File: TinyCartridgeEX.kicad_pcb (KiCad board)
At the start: 2 copper layers, 62 x 81.1 mm, 25 parts, among them U1 SN74LVC8T245, U2 SN74LVC8T245, U3 SN74LVC8T245, U4 74LV17A, U5 74LVC06A, U6 74LVC1G06, U7 74LVC2G132, U9 TinyFPGA_EX, X1 EXPANSION_PORT_C64_EDGE

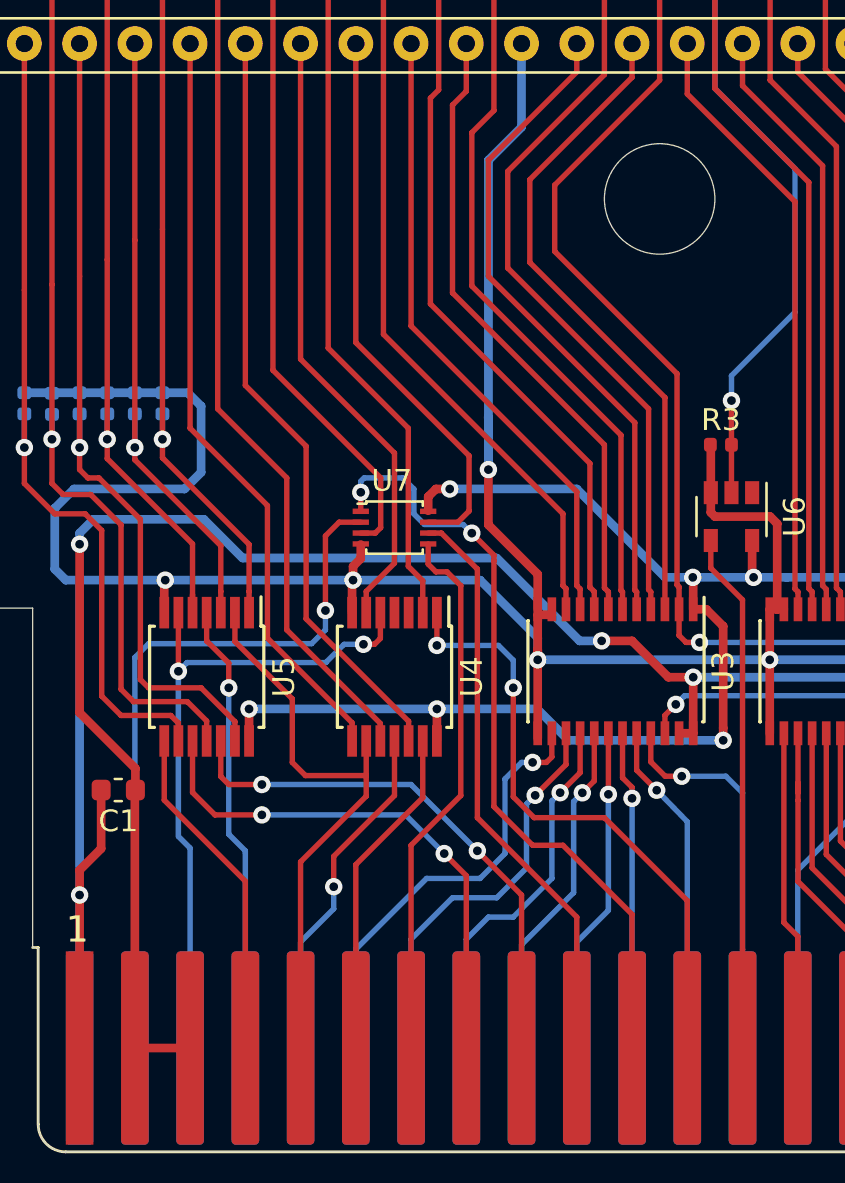
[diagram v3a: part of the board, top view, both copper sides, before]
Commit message: Replace cartridge footprint
The new footprint is created based on the technical drawings
found here:  http://wiki.icomp.de/wiki/C64_Cartridge_Cases
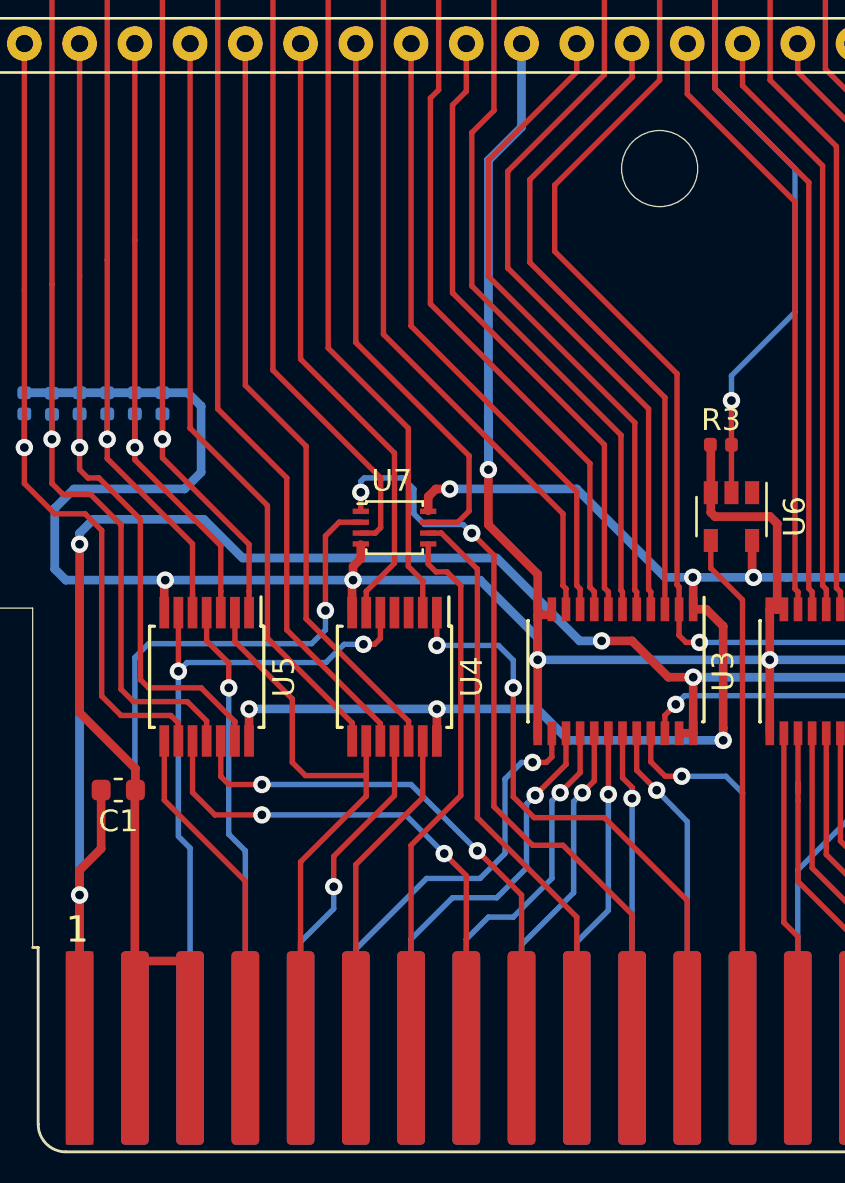
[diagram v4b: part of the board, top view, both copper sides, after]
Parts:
- CART1: footprint RETRO_Innovations:CARTRIDGE_C64 -> icomp:CARTRIDGE_C64_GERMAN
- moved CART1 45.2 mm to (76.2, 119.9)
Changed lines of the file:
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@@
     (add_net VCC)
+  )
+  (module icomp:CARTRIDGE_C64_GERMAN (layer F.Cu)
+    (at 76.2 119.888)
+    (fp_text reference CART1 (at 0 0) (layer F.SilkS) hide
+      (effects (font (size 1.27 1.27) (thickness 0.15)))
+    )
+    (fp_text value CARTRIDGE_C64 (at 0 0) (layer F.SilkS) hide
+      (effects (font (size 1.27 1.27) (thickness 0.15)))
+    )
+    (fp_circle (center 0 0) (end 2.575 0) (layer F.CrtYd) (width 1))
+    (fp_line (start -32.9 45.4) (end -32.9 -39.9) (layer Dwgs.User) (width 2.2))
+    (fp_line (start -32.9 -39.9) (end 32.9 -39.9) (layer Dwgs.User) (width 2.2))
+    (fp_line (start 32.9 -39.9) (end 32.9 45.4) (layer Dwgs.User) (width 2.2))
+    (fp_line (start 32.9 45.4) (end -32.9 45.4) (layer Dwgs.User) (width 2.2))
+    (fp_line (start -33.1 36.4) (end 33.1 36.4) (layer Dwgs.User) (width 1.8))
+    (fp_line (start -33.35 -33.85) (end -29.65 -33.85) (layer Dwgs.User) (width 1.3))
+    (fp_line (start -29.65 -33.85) (end -29.65 -24.15) (layer Dwgs.User) (width 1.3))
+    (fp_line (start -29.65 -24.15) (end -33.35 -24.15) (layer Dwgs.User) (width 1.3))
+    (fp_line (start -33.35 -24.15) (end -33.35 -33.85) (layer Dwgs.User) (width 1.3))
+    (fp_line (start -33.35 24.15) (end -29.65 24.15) (layer Dwgs.User) (width 1.3))
+    (fp_line (start -29.65 24.15) (end -29.65 33.85) (layer Dwgs.User) (width 1.3))
+    (fp_line (start -29.65 33.85) (end -33.35 33.85) (layer Dwgs.User) (width 1.3))
+    (fp_line (start -33.35 33.85) (end -33.35 24.15) (layer Dwgs.User) (width 1.3))
+    (fp_line (start 33.35 -33.85) (end 29.65 -33.85) (layer Dwgs.User) (width 1.3))
+    (fp_line (start 29.65 -33.85) (end 29.65 -24.15) (layer Dwgs.User) (width 1.3))
+    (fp_line (start 29.65 -24.15) (end 33.35 -24.15) (layer Dwgs.User) (width 1.3))
+    (fp_line (start 33.35 -24.15) (end 33.35 -33.85) (layer Dwgs.User) (width 1.3))
+    (fp_line (start 33.35 24.15) (end 29.65 24.15) (layer Dwgs.User) (width 1.3))
+    (fp_line (start 29.65 24.15) (end 29.65 33.85) (layer Dwgs.User) (width 1.3))
+    (fp_line (start 29.65 33.85) (end 33.35 33.85) (layer Dwgs.User) (width 1.3))
+    (fp_line (start 33.35 33.85) (end 33.35 24.15) (layer Dwgs.User) (width 1.3))
+    (pad "" np_thru_hole circle (at 0 0) (size 3.5 3.5) (drill 3.5) (layers *.Cu *.Mask))
   )
   (module Symbol:Symbol_CC-Attribution_CopperTop_Small (layer F.Cu)
@@
       (effects (font (size 1 1) (thickness 0.15)))
     )
-    (fp_text value Symbol_CC-Attribution_CopperTop_Small (at 0 4.064) (layer F.Fab)
+    (fp_text value Symbol_CC-Attribution_CopperTop_Small (at 0 4.064) (layer F.Fab) hide
       (effects (font (size 1 1) (thickness 0.15)))
     )
@@
       (effects (font (size 1 1) (thickness 0.15)))
     )
-    (fp_text value Symbol_CreativeCommons_CopperTop_Type2_Small (at 0.127 3.683) (layer F.Fab)
+    (fp_text value Symbol_CreativeCommons_CopperTop_Type2_Small (at 0.127 3.683) (layer F.Fab) hide
       (effects (font (size 1 1) (thickness 0.15)))
     )
@@
       (effects (font (size 1 1) (thickness 0.15)))
     )
-    (fp_text value Symbol_CC-ShareAlike_CopperTop_Small (at 0.508 3.81) (layer F.Fab)
+    (fp_text value Symbol_CC-ShareAlike_CopperTop_Small (at 0.508 3.81) (layer F.Fab) hide
       (effects (font (size 1 1) (thickness 0.15)))
     )
@@
     (fp_line (start -1.09982 1.19888) (end -0.59944 1.50114) (layer F.Cu) (width 0.381))
   )
-  (module RETRO_Innovations:CARTRIDGE_C64 (layer F.Cu)
-    (at 76.2 165.1)
-    (fp_text reference CART1 (at 0 0) (layer F.SilkS) hide
-      (effects (font (size 1.27 1.27) (thickness 0.15)))
-    )
-    (fp_text value CARTRIDGE_C64 (at 0 0) (layer F.SilkS) hide
-      (effects (font (size 1.27 1.27) (thickness 0.15)))
-    )
-    (fp_line (start -34.036 0) (end -31.4325 0) (layer Dwgs.User) (width 0.1))
-    (fp_line (start 31.4325 0) (end 34.036 0) (layer Dwgs.User) (width 0.1))
-    (fp_line (start 34.036 0) (end 34.036 -88.138) (layer Dwgs.User) (width 0.1))
-    (fp_line (start 34.036 -88.138) (end -34.036 -88.138) (layer Dwgs.User) (width 0.1))
-    (fp_line (start -34.036 -88.138) (end -34.036 0) (layer Dwgs.User) (width 0.1))
-    (fp_line (start -31.4325 -86.106) (end 31.4325 -86.106) (layer Dwgs.User) (width 0.1))
-    (fp_line (start 31.4325 -86.106) (end 31.4325 -77.5208) (layer Dwgs.User) (width 0.1))
-    (fp_line (start 31.4325 -77.5208) (end 28.8925 -77.5208) (layer Dwgs.User) (width 0.1))
-    (fp_line (start 28.8925 -77.5208) (end 28.8925 -74.295) (layer Dwgs.User) (width 0.1))
-    (fp_line (start 28.8925 -74.295) (end 31.4325 -74.295) (layer Dwgs.User) (width 0.1))
-    (fp_line (start 31.4325 -74.295) (end 31.4325 -20.1168) (layer Dwgs.User) (width 0.1))
-    (fp_line (start 31.4325 -20.1168) (end 28.8925 -20.1168) (layer Dwgs.User) (width 0.1))
-    (fp_line (start 28.8925 -20.1168) (end 28.8925 -17.526) (layer Dwgs.User) (width 0.1))
-    (fp_line (start 28.8925 -17.526) (end 31.4325 -17.526) (layer Dwgs.User) (width 0.1))
-    (fp_line (start 31.4325 -17.526) (end 31.4325 0) (layer Dwgs.User) (width 0.1))
-    (fp_line (start 31.4325 0) (end -31.4325 0) (layer Dwgs.User) (width 0.1))
-    (fp_line (start -31.4325 0) (end -31.4325 -17.526) (layer Dwgs.User) (width 0.1))
-    (fp_line (start -31.4325 -17.526) (end -28.8925 -17.526) (layer Dwgs.User) (width 0.1))
-    (fp_line (start -28.8925 -17.526) (end -28.8925 -20.1168) (layer Dwgs.User) (width 0.1))
-    (fp_line (start -28.8925 -20.1168) (end -31.4325 -20.1168) (layer Dwgs.User) (width 0.1))
-    (fp_line (start -31.4325 -20.1168) (end -31.4325 -74.295) (layer Dwgs.User) (width 0.1))
-    (fp_line (start -31.4325 -74.295) (end -28.8925 -74.295) (layer Dwgs.User) (width 0.1))
-    (fp_line (start -28.8925 -74.295) (end -28.8925 -77.5208) (layer Dwgs.User) (width 0.1))
-    (fp_line (start -28.8925 -77.5208) (end -31.4325 -77.5208) (layer Dwgs.User) (width 0.1))
-    (fp_line (start -31.4325 -77.5208) (end -31.4325 -86.106) (layer Dwgs.User) (width 0.1))
-    (pad "" np_thru_hole circle (at 0 -43.815) (size 5.08 5.08) (drill 5.08) (layers *.Cu *.Mask))
-  )
   (module Package_SO:VSSOP-8_2.4x2.1mm_P0.5mm (layer F.Cu)
     (at 64.008 136.398)
@@
       (effects (font (size 1 1) (thickness 0.15)))
     )
-    (fp_text value 74LVC2G132 (at 0 2.413) (layer F.Fab)
+    (fp_text value 74LVC2G132 (at -0.008 -2.098) (layer F.Fab)
       (effects (font (size 1 1) (thickness 0.15)))
     )
@@
       (effects (font (size 1 1) (thickness 0.15)))
     )
-    (fp_text value 4.7k (at 0 -1.27) (layer F.Fab)
+    (fp_text value 4.7k (at -0.083 1.088) (layer F.Fab)
       (effects (font (size 1 1) (thickness 0.15)))
     )
@@
       (effects (font (size 1 1) (thickness 0.15)))
     )
-    (fp_text value 4.7k (at -0.104 -1.27) (layer F.Fab)
+    (fp_text value 4.7k (at -0.023 1.014) (layer F.Fab)
       (effects (font (size 1 1) (thickness 0.15)))
     )
@@
       (effects (font (size 1 1) (thickness 0.15)))
     )
-    (fp_text value 4.7k (at 0 1.17) (layer F.Fab)
+    (fp_text value 4.7k (at 0.001 -1.141) (layer F.Fab)
       (effects (font (size 1 1) (thickness 0.15)))
     )
@@
       (effects (font (size 1 1) (thickness 0.15)))
     )
-    (fp_text value 0.1u (at 0 1.43) (layer F.Fab)
+    (fp_text value 0.1u (at 0.008 -1.437) (layer F.Fab)
       (effects (font (size 1 1) (thickness 0.15)))
     )
@@
       (effects (font (size 1 1) (thickness 0.15)))
     )
-    (fp_text value 74LVC1G06 (at 0 2.9 90) (layer F.Fab)
+    (fp_text value 74LVC1G06 (at -1.69 0.002 180) (layer F.Fab)
       (effects (font (size 1 1) (thickness 0.15)))
     )
@@
   (gr_line (start 47.371 155.702) (end 47.625 155.702) (layer Edge.Cuts) (width 0.05))
   (gr_line (start 104.775 155.702) (end 105.029 155.702) (layer Edge.Cuts) (width 0.05))
-  (segment (start 52.07 160.3248) (end 54.61 160.3248) (width 0.4) (layer F.Cu) (net 1))
   (segment (start 77.093 145.852) (end 77.743 145.852) (width 0.4) (layer F.Cu) (net 1))
   (segment (start 87.761 145.852) (end 88.411 145.852) (width 0.4) (layer F.Cu) (net 1))
@@
   (segment (start 49.53 137.16) (end 49.53 144.907) (width 0.4) (layer F.Cu) (net 1))
   (segment (start 55.245 136.017) (end 57.023 137.795) (width 0.4) (layer B.Cu) (net 1))
+  (segment (start 52.07 156.3248) (end 54.61 156.3248) (width 0.4) (layer F.Cu) (net 1))
   (segment (start 91.929 140.406) (end 92.579 140.406) (width 0.4) (layer F.Cu) (net 2))
   (segment (start 81.261 142.475) (end 81.261 145.852) (width 0.4) (layer F.Cu) (net 2))

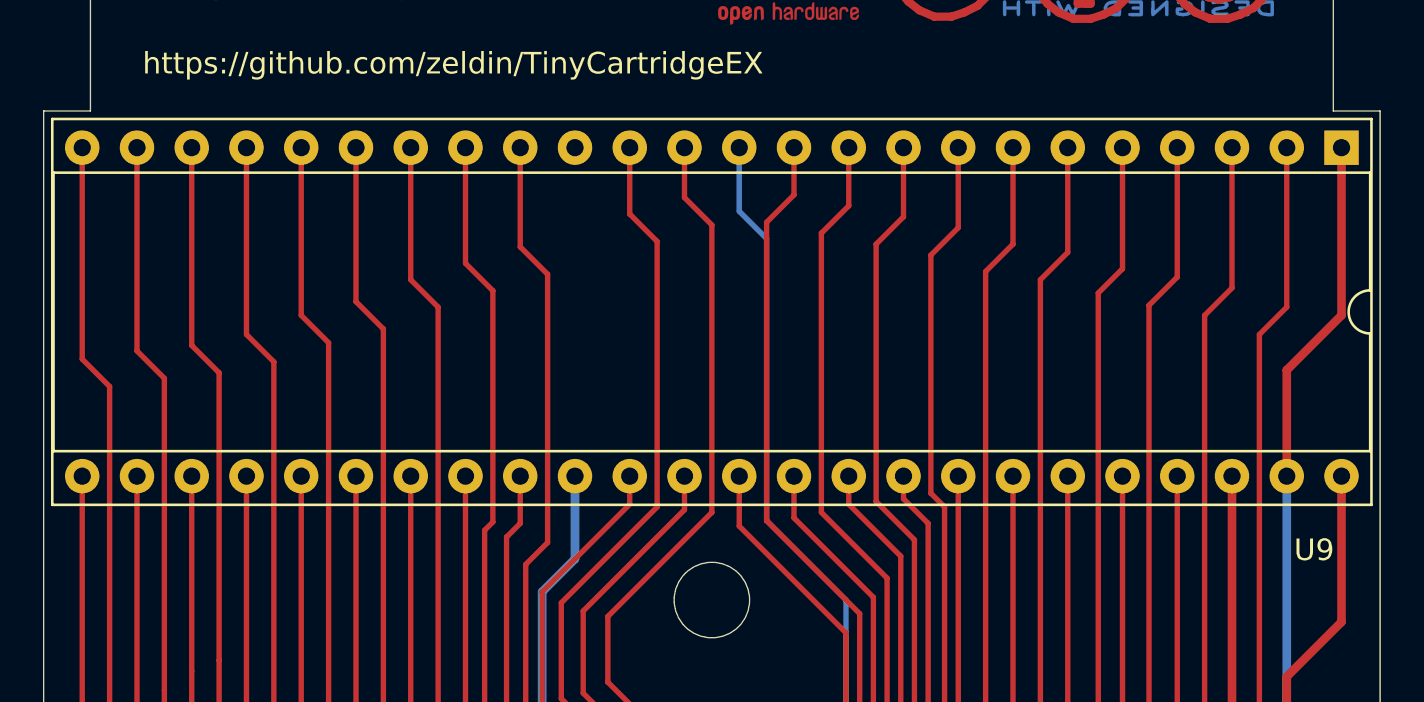
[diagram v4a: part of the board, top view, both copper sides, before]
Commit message: Insert a 3D model of the TinyFPGA EX module
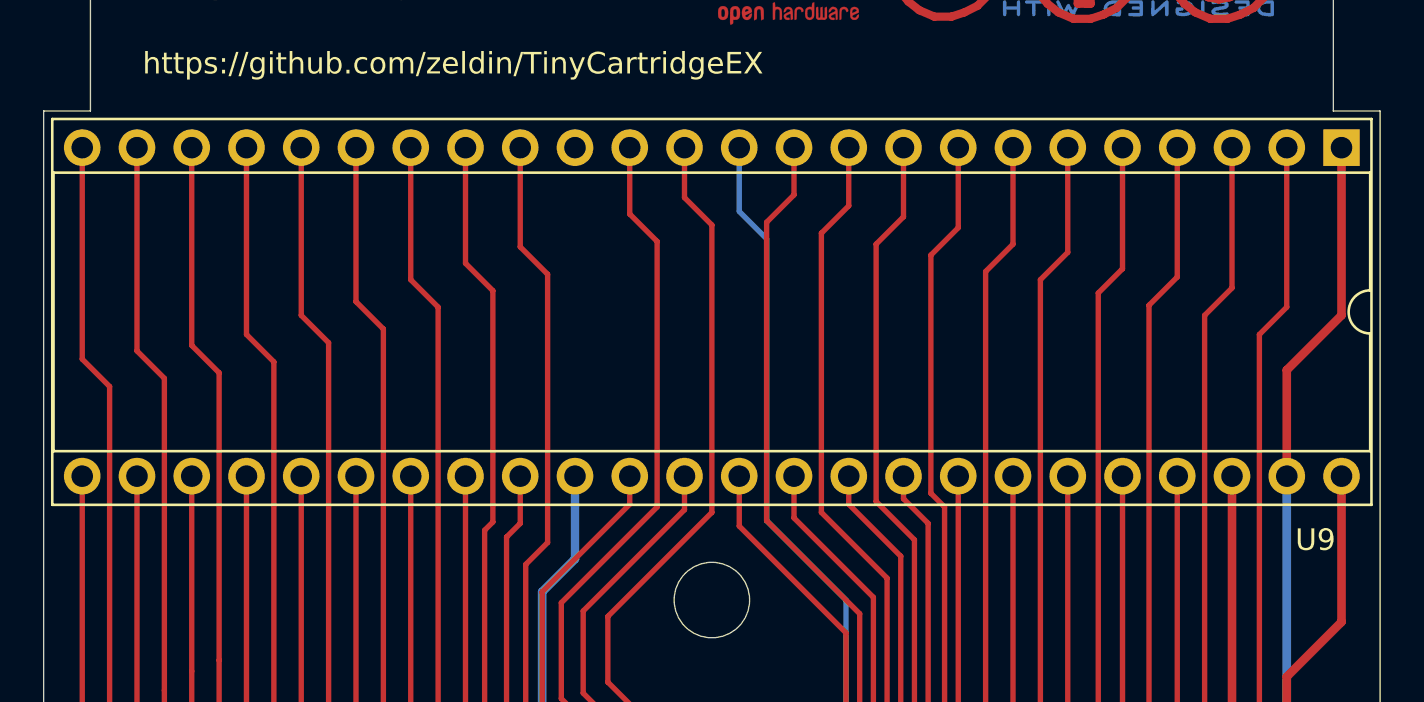
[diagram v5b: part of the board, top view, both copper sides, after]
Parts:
- added J1: Conn_01x24, PinHeader:PinHeader_1x24_P2.54mm_Vertical_UpsideDown, F.Cu at (105.4, 98.9)
- added J2: Conn_01x24, PinHeader:PinHeader_1x24_P2.54mm_Vertical_UpsideDown, F.Cu at (47.0, 114.1)
- U9: footprint Package_DIP:DIP-48_W15.24mm_Socket -> TinyFPGA:TinyFPGA_EX

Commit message: Add diode to Vin
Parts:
- added D1: EC30QSA045, Diode_SMD:D_SMA_Handsoldering, F.Cu at (104.3, 127.2)
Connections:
- U9 pad 48: +5V -> Net-(D1-Pad1)
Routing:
- net +5V: track 123.3 -> 107.2 mm
- net Net-(D1-Pad1): track 0.00 -> 11.0 mm
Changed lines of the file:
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@@
     (thickness 1.6)
     (drawings 20)
-    (tracks 723)
+    (tracks 726)
     (zones 0)
-    (modules 27)
-    (nets 85)
+    (modules 28)
+    (nets 86)
   )
   (page A4)
@@
   (net 83 "Net-(U7-Pad2)")
   (net 84 "Net-(U7-Pad1)")
+  (net 85 "Net-(D1-Pad1)")
   (net_class Default "This is the default net class."
     (clearance 0.2)
@@
     (add_net +5V)
     (add_net GND)
+    (add_net "Net-(D1-Pad1)")
     (add_net VCC)
+  )
+  (module Diode_SMD:D_SMA_Handsoldering (layer F.Cu)
+    (at 104.3 127.2 270)
+    (descr "Diode SMA (DO-214AC) Handsoldering")
+    (tags "Diode SMA (DO-214AC) Handsoldering")
+    (attr smd)
+    (fp_text reference D1 (at -0.2 2.5 90) (layer F.SilkS)
+      (effects (font (size 1 1) (thickness 0.15)))
+    )
+    (fp_text value EC30QSA045 (at 0 2.6 90) (layer F.Fab)
+      (effects (font (size 1 1) (thickness 0.15)))
+    )
+    (fp_line (start -4.4 -1.65) (end 2.5 -1.65) (layer F.SilkS) (width 0.12))
+    (fp_line (start -4.4 1.65) (end 2.5 1.65) (layer F.SilkS) (width 0.12))
+    (fp_line (start -0.64944 0.00102) (end 0.50118 -0.79908) (layer F.Fab) (width 0.1))
+    (fp_line (start -0.64944 0.00102) (end 0.50118 0.75032) (layer F.Fab) (width 0.1))
+    (fp_line (start 0.50118 0.75032) (end 0.50118 -0.79908) (layer F.Fab) (width 0.1))
+    (fp_line (start -0.64944 -0.79908) (end -0.64944 0.80112) (layer F.Fab) (width 0.1))
+    (fp_line (start 0.50118 0.00102) (end 1.4994 0.00102) (layer F.Fab) (width 0.1))
+    (fp_line (start -0.64944 0.00102) (end -1.55114 0.00102) (layer F.Fab) (width 0.1))
+    (fp_line (start -4.5 1.75) (end -4.5 -1.75) (layer F.CrtYd) (width 0.05))
+    (fp_line (start 4.5 1.75) (end -4.5 1.75) (layer F.CrtYd) (width 0.05))
+    (fp_line (start 4.5 -1.75) (end 4.5 1.75) (layer F.CrtYd) (width 0.05))
+    (fp_line (start -4.5 -1.75) (end 4.5 -1.75) (layer F.CrtYd) (width 0.05))
+    (fp_line (start 2.3 -1.5) (end -2.3 -1.5) (layer F.Fab) (width 0.1))
+    (fp_line (start 2.3 -1.5) (end 2.3 1.5) (layer F.Fab) (width 0.1))
+    (fp_line (start -2.3 1.5) (end -2.3 -1.5) (layer F.Fab) (width 0.1))
+    (fp_line (start 2.3 1.5) (end -2.3 1.5) (layer F.Fab) (width 0.1))
+    (fp_line (start -4.4 -1.65) (end -4.4 1.65) (layer F.SilkS) (width 0.12))
+    (fp_text user %R (at 0 -2.5 90) (layer F.Fab)
+      (effects (font (size 1 1) (thickness 0.15)))
+    )
+    (pad 2 smd rect (at 2.5 0 270) (size 3.5 1.8) (layers F.Cu F.Paste F.Mask)
+      (net 1 +5V))
+    (pad 1 smd rect (at -2.5 0 270) (size 3.5 1.8) (layers F.Cu F.Paste F.Mask)
+      (net 85 "Net-(D1-Pad1)"))
+    (model ${KISYS3DMOD}/Diode_SMD.3dshapes/D_SMA.wrl
+      (at (xyz 0 0 0))
+      (scale (xyz 1 1 1))
+      (rotate (xyz 0 0 0))
+    )
   )
   (module TinyFPGA:TinyFPGA_EX (layer F.Cu)
@@
     (fp_arc (start 7.62 -1.33) (end 6.62 -1.33) (angle -180) (layer F.SilkS) (width 0.12))
     (pad 48 thru_hole oval (at 15.24 0 270) (size 1.7 1.7) (drill 1) (layers *.Cu *.Mask)
-      (net 1 +5V))
+      (net 85 "Net-(D1-Pad1)"))
     (pad 24 thru_hole oval (at 0 58.42 270) (size 1.7 1.7) (drill 1) (layers *.Cu *.Mask)
       (net 65 GAME))
@@
   (segment (start 52.07 148.4885) (end 52.0955 148.463) (width 0.4) (layer F.Cu) (net 1))
   (segment (start 52.07 160.3248) (end 52.07 148.4885) (width 0.4) (layer F.Cu) (net 1))
-  (segment (start 102.87 141.986) (end 101.581 143.275) (width 0.4) (layer F.Cu) (net 1))
-  (segment (start 101.581 143.275) (end 99.079 143.275) (width 0.4) (layer F.Cu) (net 1))
-  (segment (start 102.87 123.444) (end 102.87 141.986) (width 0.4) (layer F.Cu) (net 1))
-  (segment (start 105.41 120.904) (end 102.87 123.444) (width 0.4) (layer F.Cu) (net 1))
-  (segment (start 105.41 120.904) (end 105.41 114.141) (width 0.4) (layer F.Cu) (net 1))
+  (segment (start 105.41 120.904) (end 105.41 114.141) (width 0.4) (layer F.Cu) (net 85))
+  (segment (start 104.3 124.7) (end 104.3 122.014) (width 0.4) (layer F.Cu) (net 85))
+  (segment (start 104.3 122.014) (end 105.41 120.904) (width 0.4) (layer F.Cu) (net 85))
   (segment (start 52.0955 147.4725) (end 52.0955 148.463) (width 0.4) (layer F.Cu) (net 1))
   (segment (start 49.53 144.907) (end 52.0955 147.4725) (width 0.4) (layer F.Cu) (net 1))
@@
   (segment (start 55.245 136.017) (end 57.023 137.795) (width 0.4) (layer B.Cu) (net 1))
   (segment (start 52.07 156.3248) (end 54.61 156.3248) (width 0.4) (layer F.Cu) (net 1))
+  (segment (start 102.9 141.956) (end 101.581 143.275) (width 0.4) (layer F.Cu) (net 1))
+  (segment (start 101.581 143.275) (end 99.079 143.275) (width 0.4) (layer F.Cu) (net 1))
+  (segment (start 102.9 135.1) (end 102.9 141.956) (width 0.4) (layer F.Cu) (net 1))
+  (segment (start 104.3 129.7) (end 104.3 133.7) (width 0.4) (layer F.Cu) (net 1))
+  (segment (start 104.3 133.7) (end 102.9 135.1) (width 0.4) (layer F.Cu) (net 1))
   (segment (start 91.929 140.406) (end 92.579 140.406) (width 0.4) (layer F.Cu) (net 2))
   (segment (start 81.261 142.475) (end 81.261 145.852) (width 0.4) (layer F.Cu) (net 2))
